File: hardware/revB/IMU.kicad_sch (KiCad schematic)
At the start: 31 parts, among them U3 IAM-20380, U4 IAM-20380, U5 PCA9543APW,118, U6 MMC5983MA, U7 MMC5983MA, U8 MXC6655XA, U9 MXC6655XA

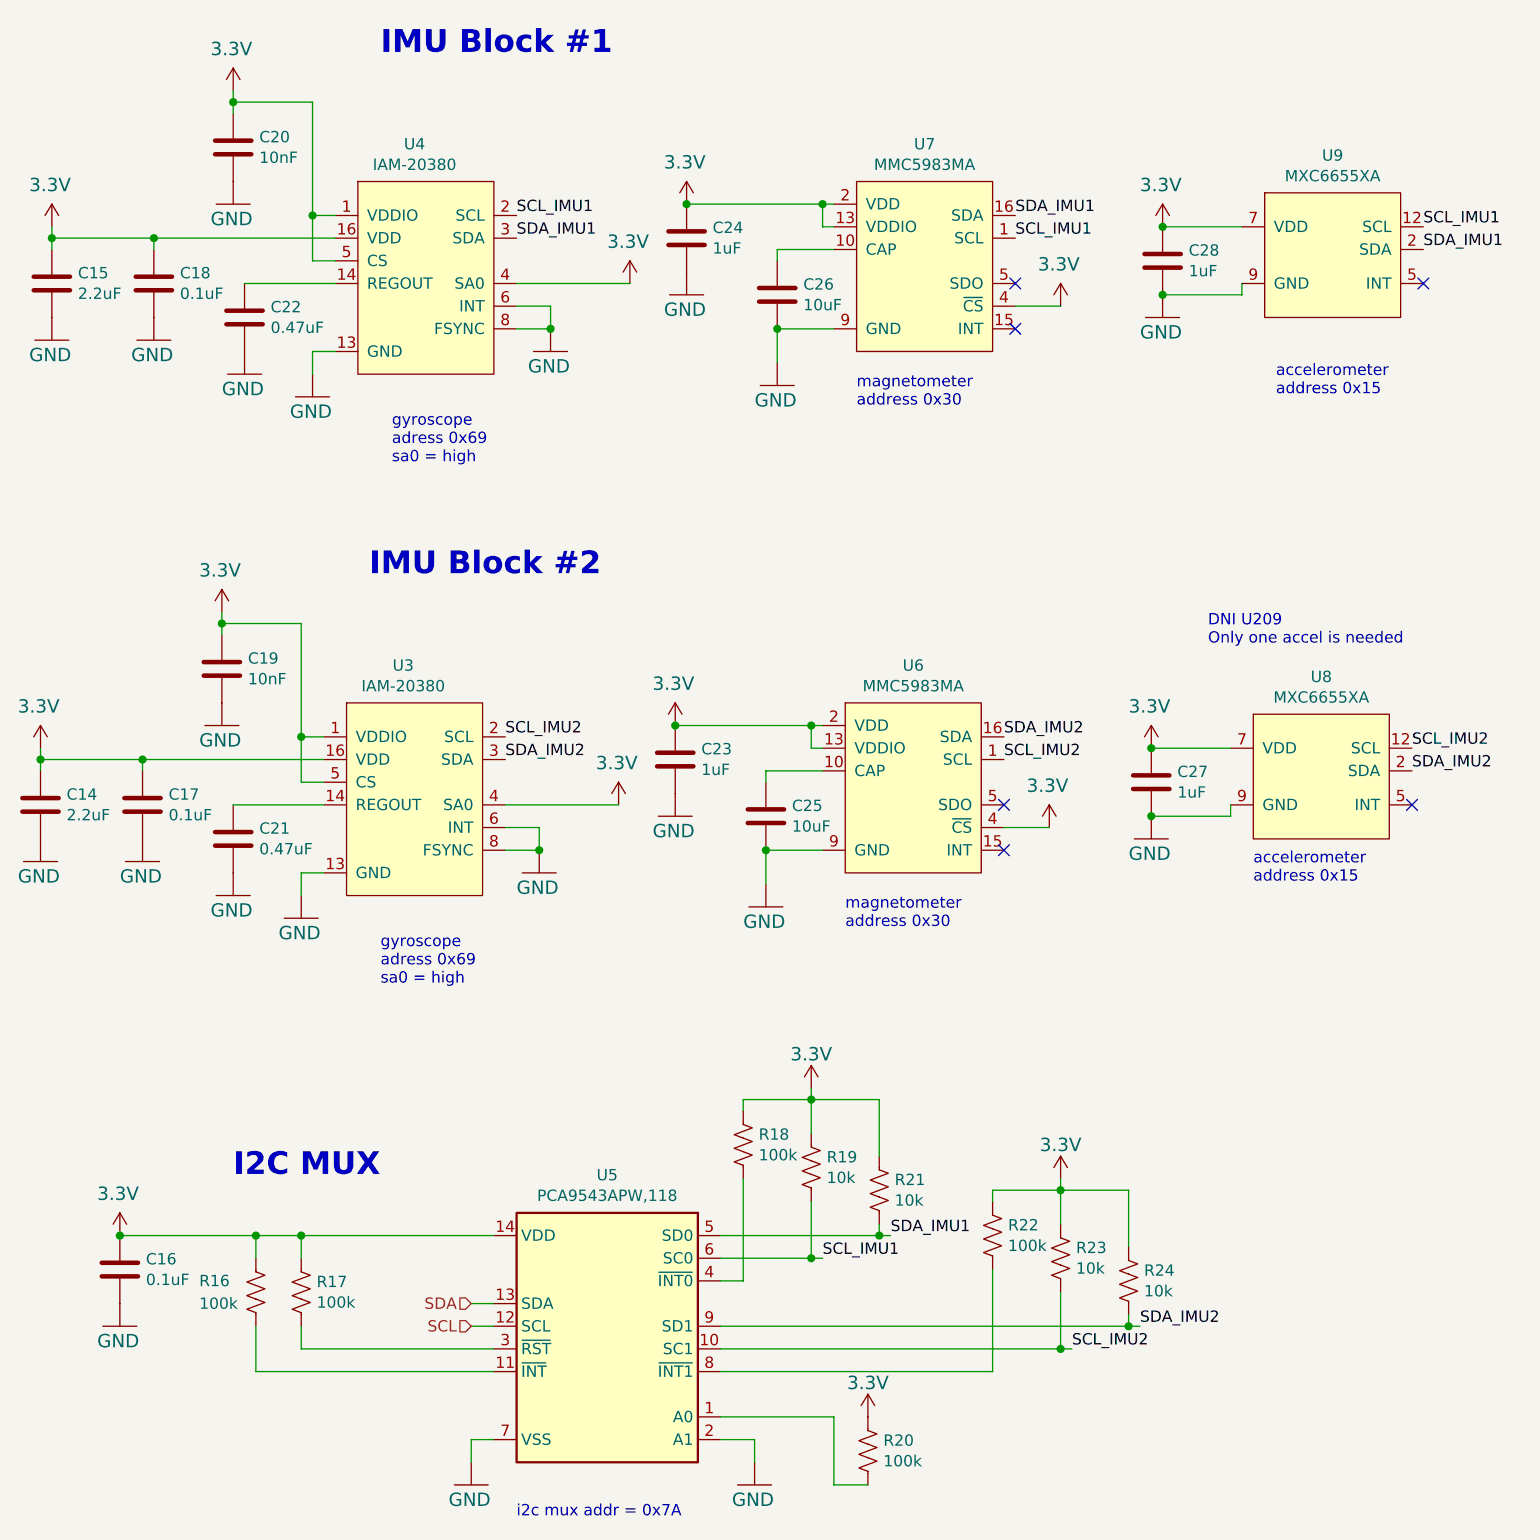
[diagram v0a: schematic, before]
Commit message: set resistor values for imu-stamp addressing
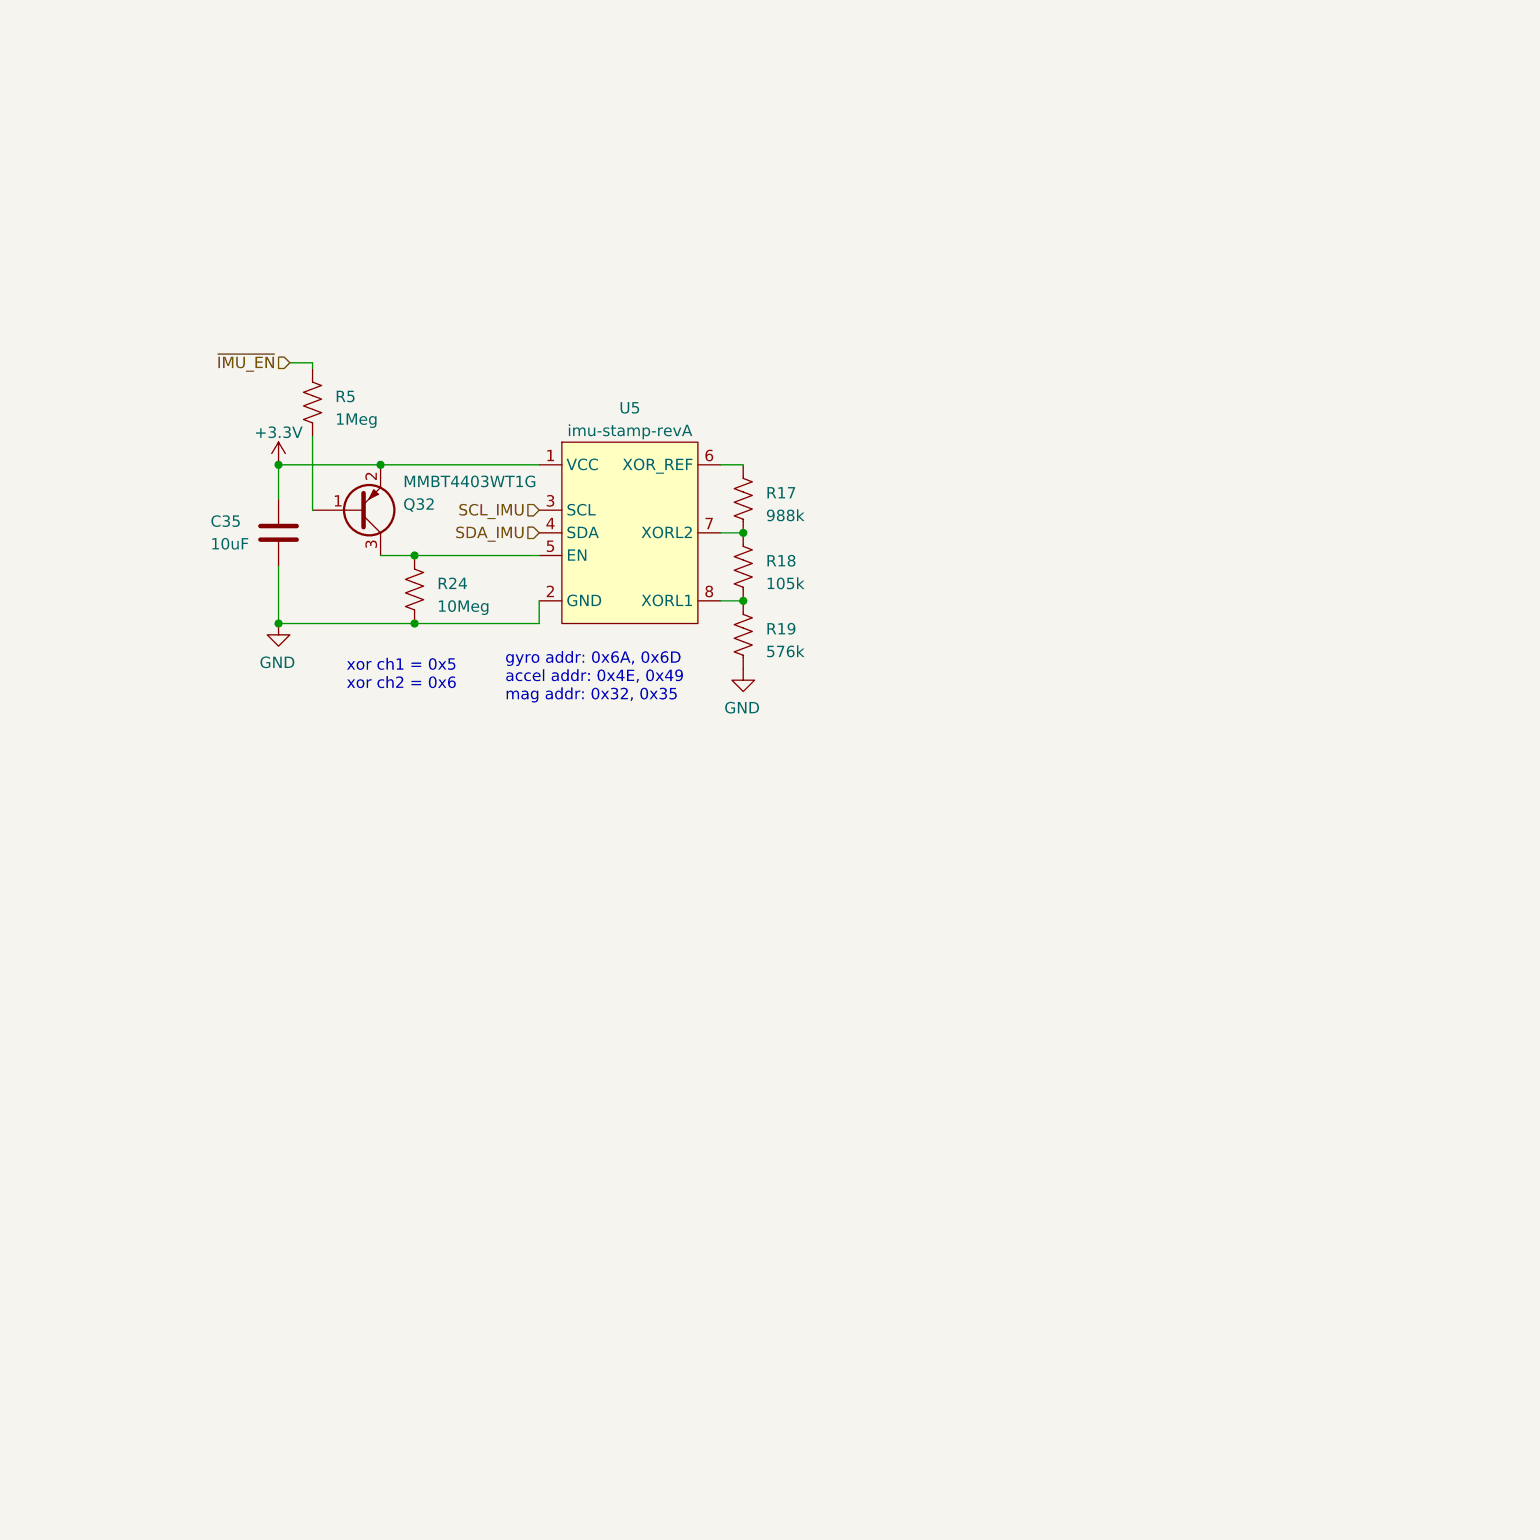
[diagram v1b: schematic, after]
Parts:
- removed C14, C15: 2.2uF, Capacitor_SMD:C_0805_2012Metric, symbol Device:C
- removed C16, C17, C18: 0.1uF, Capacitor_SMD:C_0603_1608Metric, symbol Device:C
- removed C19, C20: 10nF, Capacitor_SMD:C_0603_1608Metric, symbol Device:C
- removed C21, C22: 0.47uF, Capacitor_SMD:C_0603_1608Metric, symbol Device:C
- removed C23, C24, C27, C28: 1uF, Capacitor_SMD:C_0603_1608Metric, symbol Device:C
- removed C25, C26: 10uF, Capacitor_SMD:C_0805_2012Metric, symbol Device:C
- removed R16, R20, R22: 100k, Resistor_SMD:R_0603_1608Metric, symbol Device:R_US
- removed R21, R23: 10k, Resistor_SMD:R_0603_1608Metric, symbol Device:R_US
- removed U3, U4: IAM-20380, payload-interface-board:IAM-20380, symbol mainboard_SLI:IAM-20380
- removed U5: PCA9543APW,118, Package_SO:TSSOP-14_4.4x5mm_P0.65mm, symbol mainboard_SLI:PCA9543APW,118
- removed U6, U7: MMC5983MA, payload-interface-board:MMC5983MA, symbol mainboard_SLI:MMC5983MA
- removed U8, U9: MXC6655XA, payload-interface-board:MXC6655XA, symbol mainboard_SLI:MXC6655XA
- added C35: 10uF, Capacitor_SMD:C_0805_2012Metric, symbol Device:C
- added Q32: MMBT4403WT1G, Package_TO_SOT_SMD:SOT-323_SC-70, symbol mainboard-rescue:Q_PNP_BEC-Device-mainboard-rescue
- added R5: 1Meg, Resistor_SMD:R_0603_1608Metric, symbol Device:R_US
- added U5: imu-stamp-revA, payload-interface-board:imu-stamp-revA-SMD, symbol FP-Interface-Card:imu-stamp-revA
- R17: value 100k -> 988k
- R18: value 100k -> 105k
- R19: value 10k -> 576k
- R24: value 10k -> 10Meg
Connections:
- net SCL_IMU1 is gone; now on net GND: R19.2
- net SDA_IMU2 is gone; now on net GND: R24.2
- net GND: now also C35.2, U5.10 (GND), U5.2 (GND), U5.9 (GND)
- net at R18.2: now also R19.1, U5.8 (XORL1)
- net at R17.2: now also R18.1, U5.7 (XORL2)
- removed net 3.3V: R17.1, R18.1, R19.1, R24.1
- new net: Q32.3 (C), R24.1, U5.5 (EN)
- new net: R17.1, U5.6 (XOR_REF)
- new net: Q32.1 (B), R5.2
- new net +3V3: C35.1, Q32.2 (E), U5.1 (VCC)
- new net SCL_IMU: U5.3 (SCL)
- new net SDA_IMU: U5.4 (SDA)
- new net ~{IMU_EN}: R5.1
- no-connect marks 6 -> 0
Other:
- note added: "gyro addr: 0x6A, 0x6D accel addr: 0x4E, 0x49 mag addr: 0x32, 0x35"
- note added: "xor ch1 = 0x5 xor ch2 = 0x6"
- note removed: "DNI U209 Only one accel is needed"
- note removed: "I2C MUX"
- note removed: "IMU Block #1"
- note removed: "IMU Block #2"
- note removed: "accelerometer address 0x15"
- note removed: "gyroscope adress 0x69 sa0 = high"
- note removed: "i2c mux addr = 0x7A"
- note removed: "magnetometer address 0x30"

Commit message: updated files
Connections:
- net +3V3 renamed +3.3V
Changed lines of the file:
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@@
 (kicad_sch (version 20230121) (generator eeschema)
   (paper "A4")
+  (title_block
+    (rev "B")
+  )
   (junction (at 110.49 83.82) (diameter 0) (color 0 0 0 0)
   )
@@
     (pin "1")
     (instances
-      (project "FP Interface Card"
+      (project "payload-interface-board"
         (path "/dc2801a1-d539-4721-b31f-fe196b9f13df"
           (reference "#PWR032") (unit 1)
         )
         (path "/dc2801a1-d539-4721-b31f-fe196b9f13df/769431f6-f572-418f-b1fe-b44bee132392"
-          (reference "#PWR0112") (unit 1)
+          (reference "#PWR094") (unit 1)
         )
       )
@@
     (pin "2")
     (instances
-      (project "FP Interface Card"
+      (project "payload-interface-board"
         (path "/dc2801a1-d539-4721-b31f-fe196b9f13df"
           (reference "R19") (unit 1)
         )
         (path "/dc2801a1-d539-4721-b31f-fe196b9f13df/769431f6-f572-418f-b1fe-b44bee132392"
-          (reference "R19") (unit 1)
+          (reference "R58") (unit 1)
         )
       )
@@
     (pin "2")
     (instances
-      (project "FP Interface Card"
+      (project "payload-interface-board"
         (path "/dc2801a1-d539-4721-b31f-fe196b9f13df"
           (reference "R18") (unit 1)
         )
         (path "/dc2801a1-d539-4721-b31f-fe196b9f13df/769431f6-f572-418f-b1fe-b44bee132392"
-          (reference "R18") (unit 1)
+          (reference "R56") (unit 1)
         )
       )
@@
         )
       )
-      (project "FP Interface Card"
+      (project "payload-interface-board"
         (path "/dc2801a1-d539-4721-b31f-fe196b9f13df"
           (reference "R15") (unit 1)
         )
         (path "/dc2801a1-d539-4721-b31f-fe196b9f13df/769431f6-f572-418f-b1fe-b44bee132392"
-          (reference "R15") (unit 1)
+          (reference "R57") (unit 1)
         )
       )
@@
     (pin "2")
     (instances
-      (project "FP Interface Card"
+      (project "payload-interface-board"
         (path "/dc2801a1-d539-4721-b31f-fe196b9f13df/66fbc293-b490-4097-aa2e-a081509eef04"
           (reference "C35") (unit 1)
@@
         )
         (path "/dc2801a1-d539-4721-b31f-fe196b9f13df/769431f6-f572-418f-b1fe-b44bee132392"
-          (reference "C4") (unit 1)
+          (reference "C43") (unit 1)
         )
       )
@@
     (pin "9")
     (instances
-      (project "FP Interface Card"
+      (project "payload-interface-board"
         (path "/dc2801a1-d539-4721-b31f-fe196b9f13df"
           (reference "U5") (unit 1)
         )
         (path "/dc2801a1-d539-4721-b31f-fe196b9f13df/769431f6-f572-418f-b1fe-b44bee132392"
-          (reference "U5") (unit 1)
+          (reference "U19") (unit 1)
         )
       )
@@
     (pin "1")
     (instances
-      (project "FP Interface Card"
+      (project "payload-interface-board"
         (path "/dc2801a1-d539-4721-b31f-fe196b9f13df"
           (reference "#PWR026") (unit 1)
         )
         (path "/dc2801a1-d539-4721-b31f-fe196b9f13df/769431f6-f572-418f-b1fe-b44bee132392"
-          (reference "#PWR04") (unit 1)
+          (reference "#PWR092") (unit 1)
         )
       )
@@
     (pin "1")
     (instances
-      (project "FP Interface Card"
+      (project "payload-interface-board"
         (path "/dc2801a1-d539-4721-b31f-fe196b9f13df"
           (reference "#PWR027") (unit 1)
         )
         (path "/dc2801a1-d539-4721-b31f-fe196b9f13df/769431f6-f572-418f-b1fe-b44bee132392"
-          (reference "#PWR0111") (unit 1)
+          (reference "#PWR093") (unit 1)
         )
       )
@@
     (pin "2")
     (instances
-      (project "FP Interface Card"
+      (project "payload-interface-board"
         (path "/dc2801a1-d539-4721-b31f-fe196b9f13df"
           (reference "R17") (unit 1)
         )
         (path "/dc2801a1-d539-4721-b31f-fe196b9f13df/769431f6-f572-418f-b1fe-b44bee132392"
-          (reference "R17") (unit 1)
+          (reference "R55") (unit 1)
         )
       )
@@
         )
       )
-      (project "FP Interface Card"
+      (project "payload-interface-board"
         (path "/dc2801a1-d539-4721-b31f-fe196b9f13df"
           (reference "Q5") (unit 1)
         )
         (path "/dc2801a1-d539-4721-b31f-fe196b9f13df/769431f6-f572-418f-b1fe-b44bee132392"
-          (reference "Q5") (unit 1)
+          (reference "Q12") (unit 1)
         )
       )
@@
         )
       )
-      (project "FP Interface Card"
+      (project "payload-interface-board"
         (path "/dc2801a1-d539-4721-b31f-fe196b9f13df"
           (reference "R13") (unit 1)
         )
         (path "/dc2801a1-d539-4721-b31f-fe196b9f13df/769431f6-f572-418f-b1fe-b44bee132392"
-          (reference "R13") (unit 1)
-        )
-      )
+          (reference "R54") (unit 1)
+        )
+      )

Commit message: working
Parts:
- removed Q32: MMBT4403WT1G, Package_TO_SOT_SMD:SOT-323_SC-70, symbol mainboard-rescue:Q_PNP_BEC-Device-mainboard-rescue
- removed R24: 10Meg, Resistor_SMD:R_0603_1608Metric, symbol Device:R_US
- removed R5: 1Meg, Resistor_SMD:R_0603_1608Metric, symbol Device:R_US
- added R18: 10k, Resistor_SMD:R_0603_1608Metric, symbol Device:R_US
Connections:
- net at U5.5 (EN): now also R18.2
- net +3.3V renamed VCC
- new net IMU_EN: R18.1
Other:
- added sheet I2C-Protection-1 (I2C-Protection.kicad_sch)
- note added: "double check"
- title: (none) -> Foras Promineo Payload Interface Board
- moved on the sheet: C35, R17, R18, R19, U5
